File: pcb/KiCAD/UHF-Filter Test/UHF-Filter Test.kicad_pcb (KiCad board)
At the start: 4 copper layers, 38.1 x 20.3 mm, 18 parts, among them J1 Antenna, J2 SMA, J3 Radio, J4 SMA

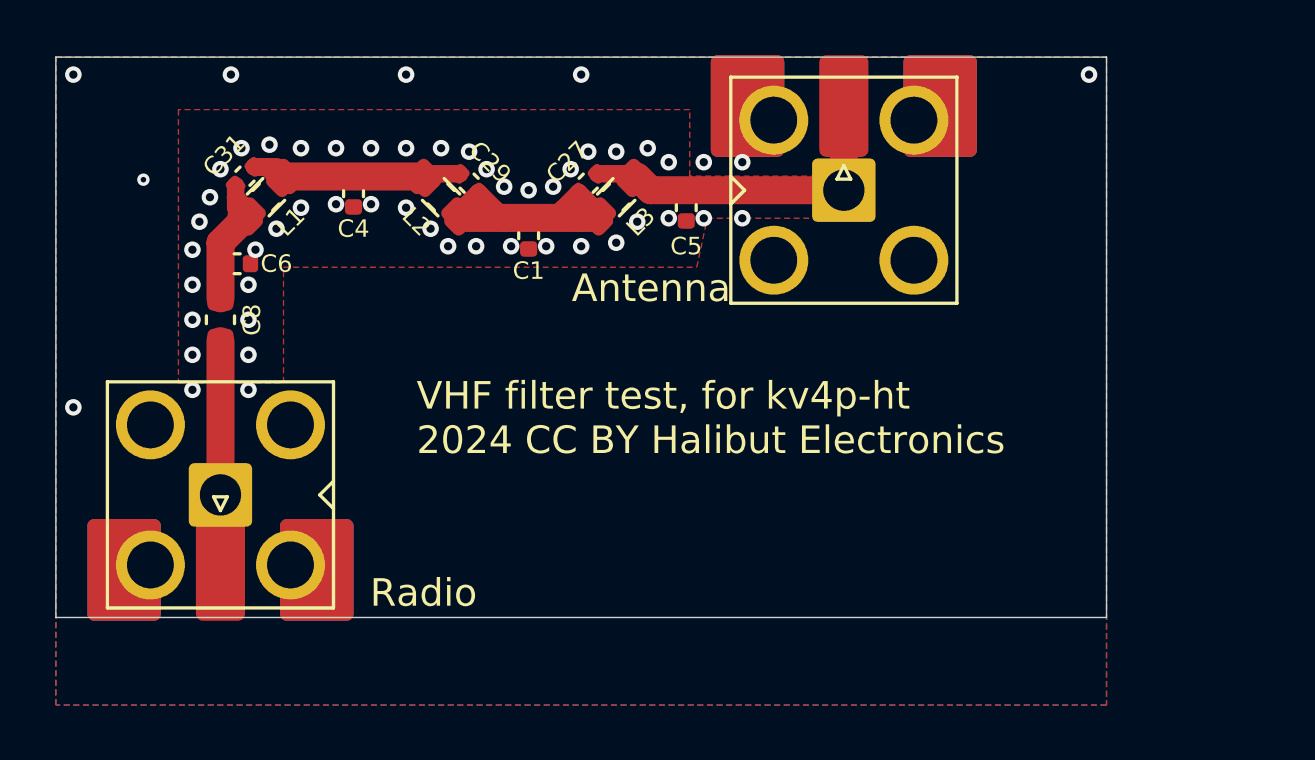
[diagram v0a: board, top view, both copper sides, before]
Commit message: Split Filter\ Test into VHF and UHF versions. Order VHF yesterday, UHF today. #22
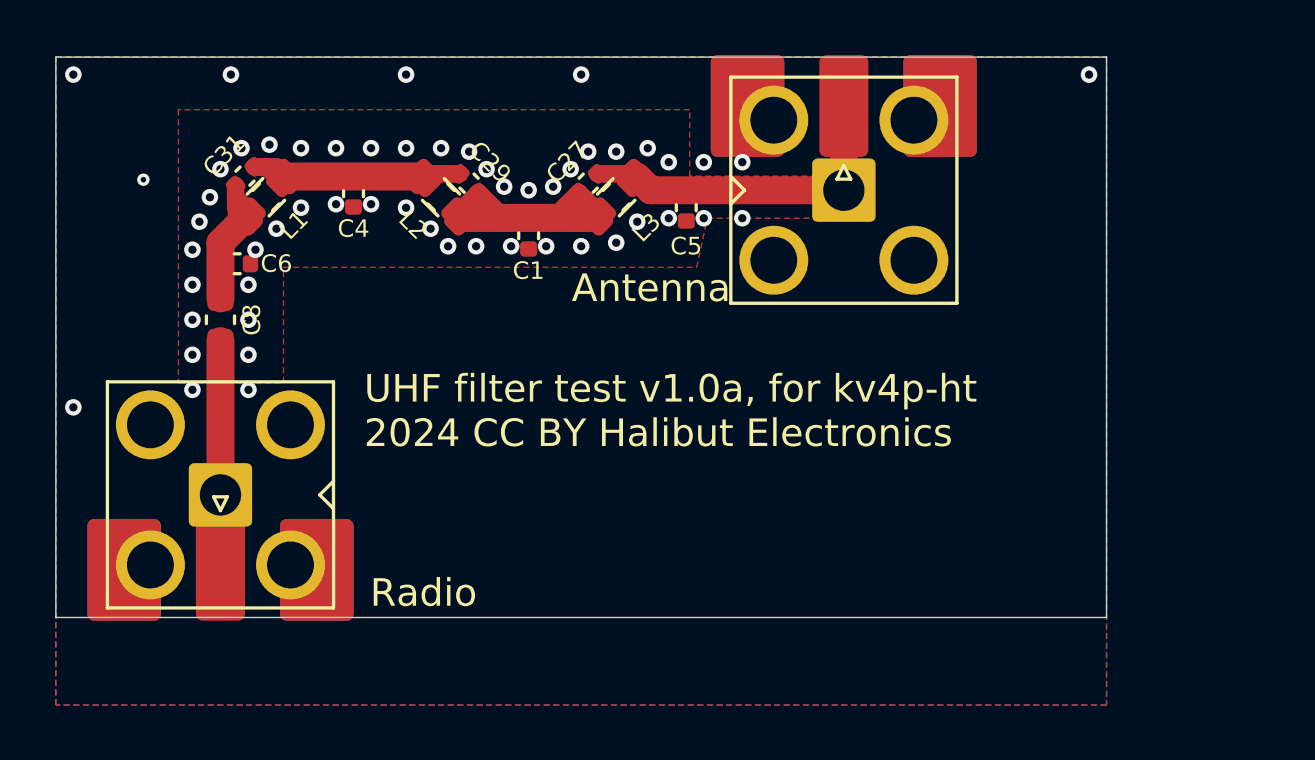
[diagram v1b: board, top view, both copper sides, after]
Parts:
- removed L4: ~, Inductor_SMD:L_0805_2012Metric
- removed L5, L6: ~, Inductor_SMD:L_0603_1608Metric
- added L14: ~, Inductor_SMD:L_0603_1608Metric, F.Cu at (147.3, 68.6)
- added L16: ~, Inductor_SMD:L_0805_2012Metric, F.Cu at (141.0, 68.6)
- added L18: ~, Inductor_SMD:L_0805_2012Metric, F.Cu at (134.6, 68.6)
- C1: value 18pF -> 6.2pF
- C27: value 2.7pF -> 0.9pF
- C29: value 13pF -> 4.7pF
- C31: value 11pF -> 3.6pF
- C4: value 16pF -> 5.1pF
- C5: value 10pF -> 3.3pF
- C6: value 5.1pF -> 1.6pF
- C8: value 2.2nF Tuned VHF -> 220pF Tuned UHF
- L1: value 27nH -> 9.1nH; footprint Inductor_SMD:L_0805_2012Metric -> Inductor_SMD:L_0603_1608Metric
- L2: value 30nH -> 9.1nH; footprint Inductor_SMD:L_0805_2012Metric -> Inductor_SMD:L_0603_1608Metric
- L3: value 43nH -> 15nH; footprint Inductor_SMD:L_0603_1608Metric -> Inductor_SMD:L_0805_2012Metric
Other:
- board text added: "UHF filter test v1.0a, for kv4p-ht 2024 CC BY Halibut Electronics"
- board text removed: "VHF filter test, for kv4p-ht 2024 CC BY Halibut Electronics"
